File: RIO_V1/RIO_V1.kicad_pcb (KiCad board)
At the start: 2 copper layers, 34 x 34 mm, 9 parts, among them J1 POGO_Conn, SW1 TL1105SF160Q, SW2 TL1105SF160Q, U2 NanoS3

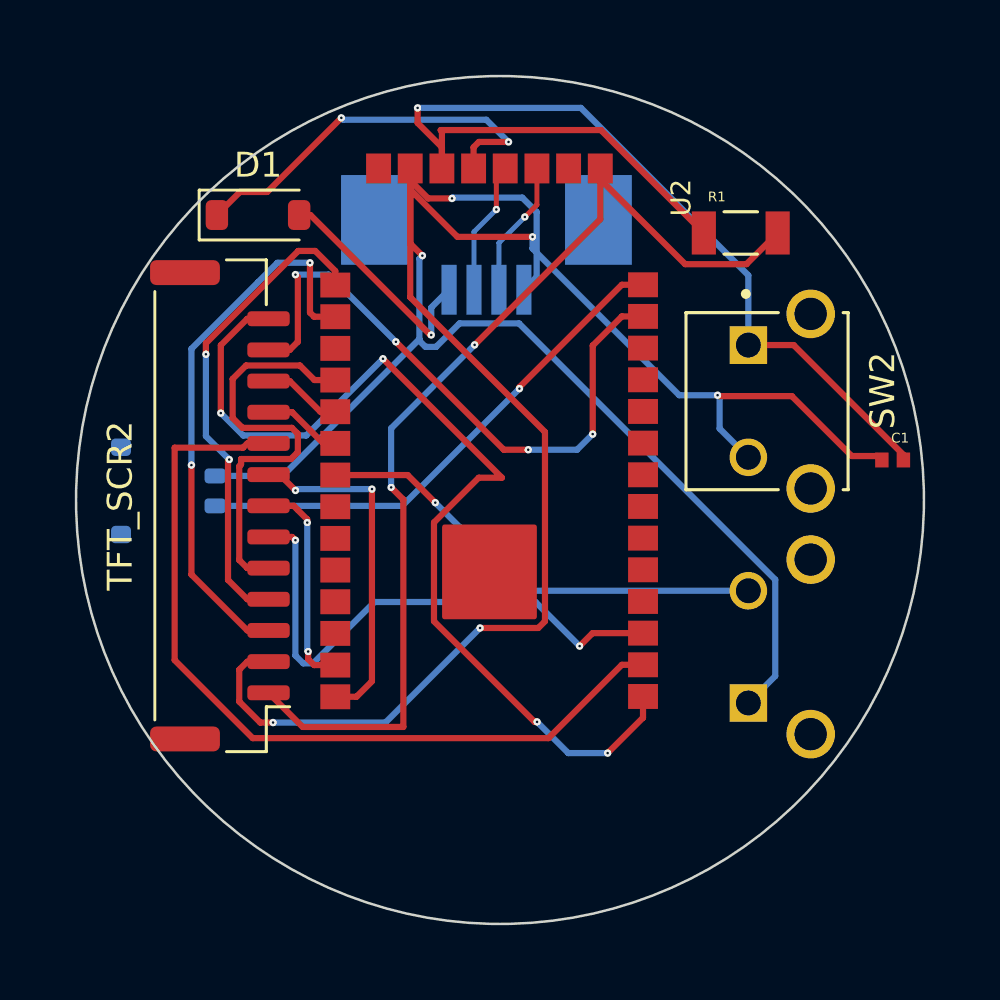
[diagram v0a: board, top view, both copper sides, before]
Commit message: Updated Symbols Footrprints and Routing
Updated the symbols, footprints and the PCB routing to work with the new resistors and ADC circuit
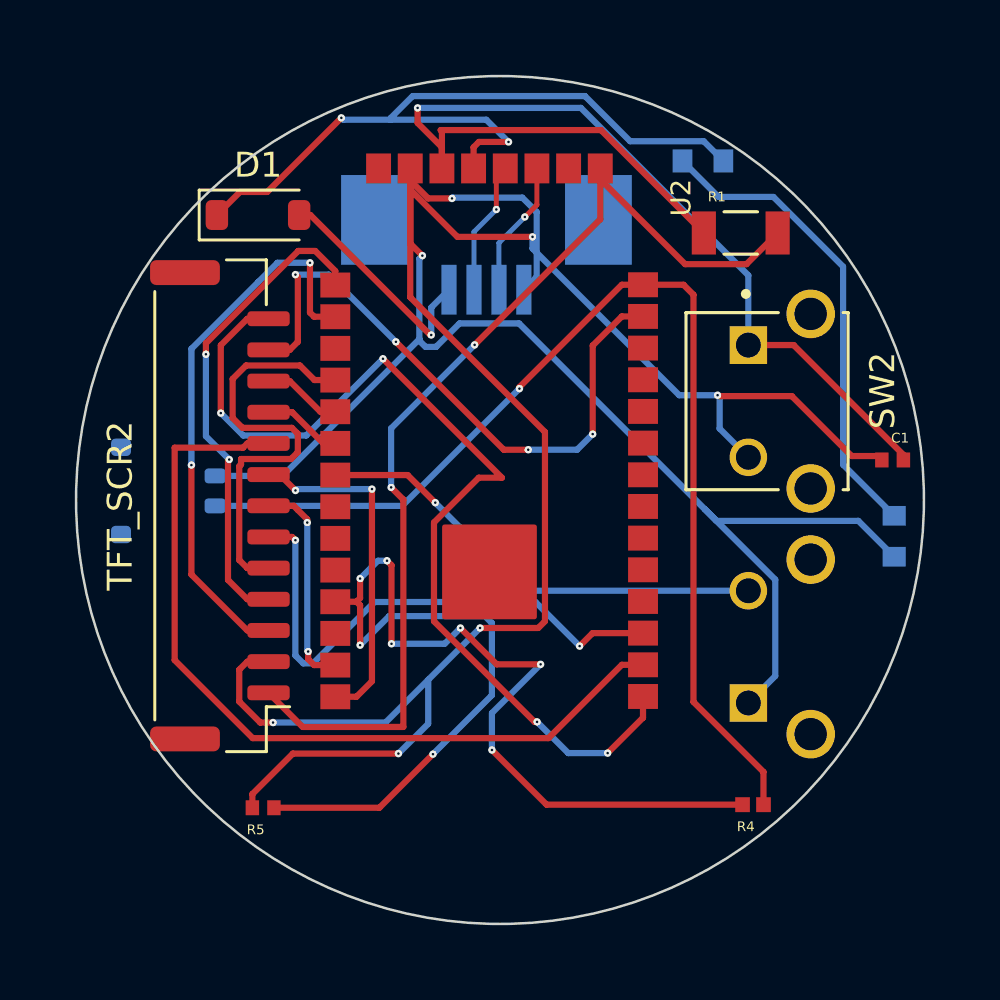
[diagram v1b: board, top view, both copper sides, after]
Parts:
- added R2: 50k, RT0603BRD0750KL:RESC1608X55N, B.Cu at (140.4, 80.4)
- added R3: 50k, RT0603BRD0750KL:RESC1608X55N, B.Cu at (148.1, 95.4)
- added R4: 442k, RMCF0402FT442K:RESC1005X35N, F.Cu at (142.4, 106.2)
- added R5: 160k, RC0402FR-07160KL:RESC1005X40N, F.Cu at (122.8, 106.3)
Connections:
- U2 pad 1: unconnected-(U2-STAT-Pad1) -> STAT
- U2 pad 33: unconnected-(U2-IO1-Pad33) -> IO1
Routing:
- net IO1: track 0.00 -> 49.8 mm, vias 0 -> 8
- net VBAT: track 20.9 -> 44.7 mm
- net IO17: track 0.00 -> 19.0 mm
- net GND: track 116.1 -> 135.0 mm, vias 6 -> 7
- net +5V: track 16.0 -> 30.9 mm

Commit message: Changed The FPC Connector To A Smaller Pitch
Changed the FPC connector on the PCB so that the pitch is reduced and overall footprint is minimized as much as possible
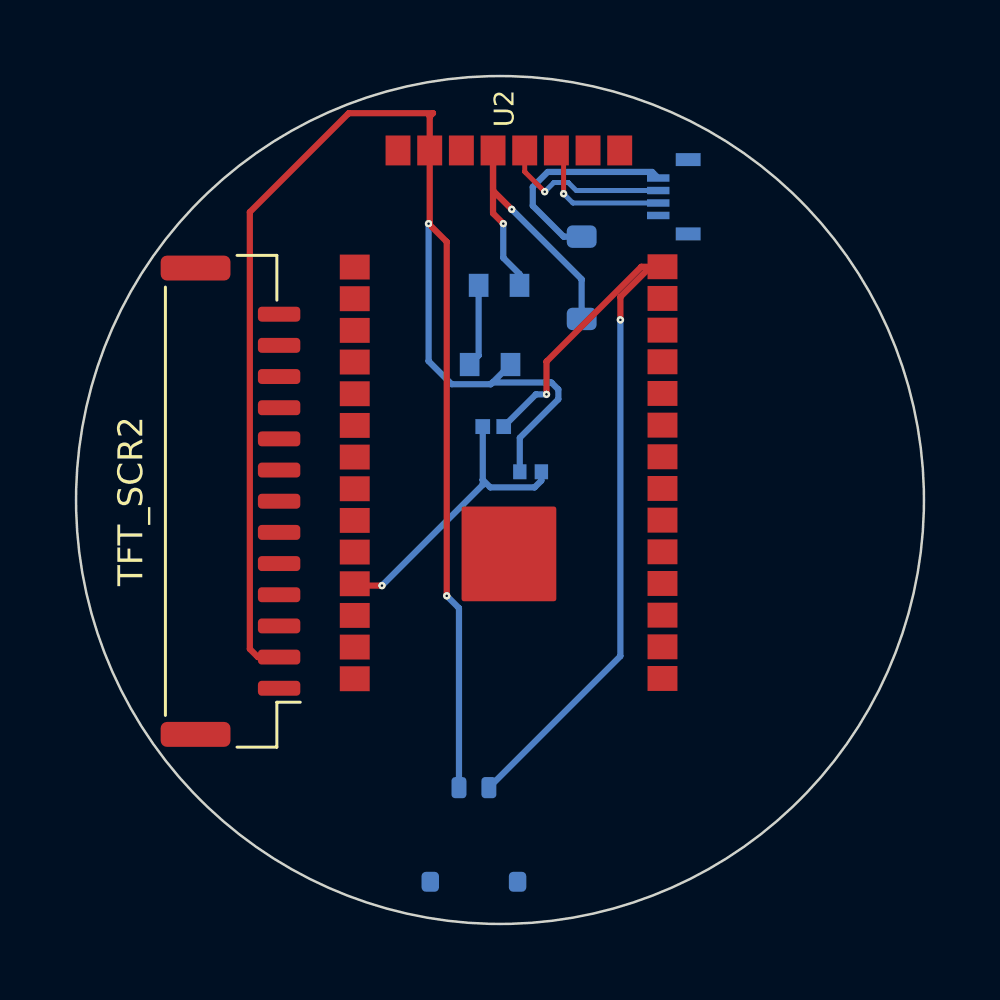
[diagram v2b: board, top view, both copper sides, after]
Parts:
- removed C1: JMK105BJ105KV-F, JMK105BJ105KV-F:CAPC1005X55N
- removed R1: RC1206FR-0710KL, RC1206FR-0710KL:RESC3116X65N
- removed SW1, SW2: TL1105SF160Q, TL1105SF160Q:SW_TL1105SF160Q
- D1, R4, R5: moved to B.Cu
- J1: footprint Connector_FFC-FPC:TE_84952-4_1x04-1MP_P1.0mm_Horizontal -> Connector:AMPHENOL_59453-042110ECHLF
- moved BT2 18.4 mm to (131.2, 107.4), turned to 180 degrees
- moved R4 18.4 mm to (132.0, 91.0)
- moved R3 17.6 mm to (131.9, 88.5), turned to 0 degrees
- moved R5 17.2 mm to (133.5, 92.8)
- moved D1 13.2 mm to (135.6, 85.1), turned to 90 degrees
- moved R2 9.58 mm to (132.2, 85.4)
- moved J1 8.32 mm to (139.8, 81.8), turned to -90 degrees
- moved U2 1.06 mm to (126.4, 79.9)
- moved TFT_SCR2 0.46 mm to (121.5, 94.0)
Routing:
- net GND: track 135.0 -> 71.7 mm, vias 7 -> 2
- net RESET: track 43.7 -> 0.00 mm, vias 1 -> 0
- net +3V3: track 41.5 -> 0.00 mm, vias 2 -> 0
- net IO5: track 39.4 -> 0.00 mm, vias 4 -> 0
- net IO1: track 49.8 -> 12.1 mm, vias 8 -> 1
- net IO6: track 33.7 -> 0.00 mm
- net IO21: track 25.2 -> 0.00 mm, vias 4 -> 0
- net IO37: track 22.3 -> 0.00 mm, vias 2 -> 0
- net IO7: track 21.8 -> 0.00 mm, vias 2 -> 0
- net IO35: track 19.5 -> 0.00 mm, vias 2 -> 0
- net IO0: track 18.5 -> 0.00 mm, vias 1 -> 0
- net IO34: track 17.5 -> 0.00 mm
- net +5V: track 30.9 -> 14.1 mm
- net IO17: track 19.0 -> 3.33 mm
- net IO4: track 13.9 -> 0.00 mm, vias 2 -> 0
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
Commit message: Added New PCB Conenctors, Routes, Components
Added new PCB components to reduce the height, changed the traces and adjusted for the battery in the PCB
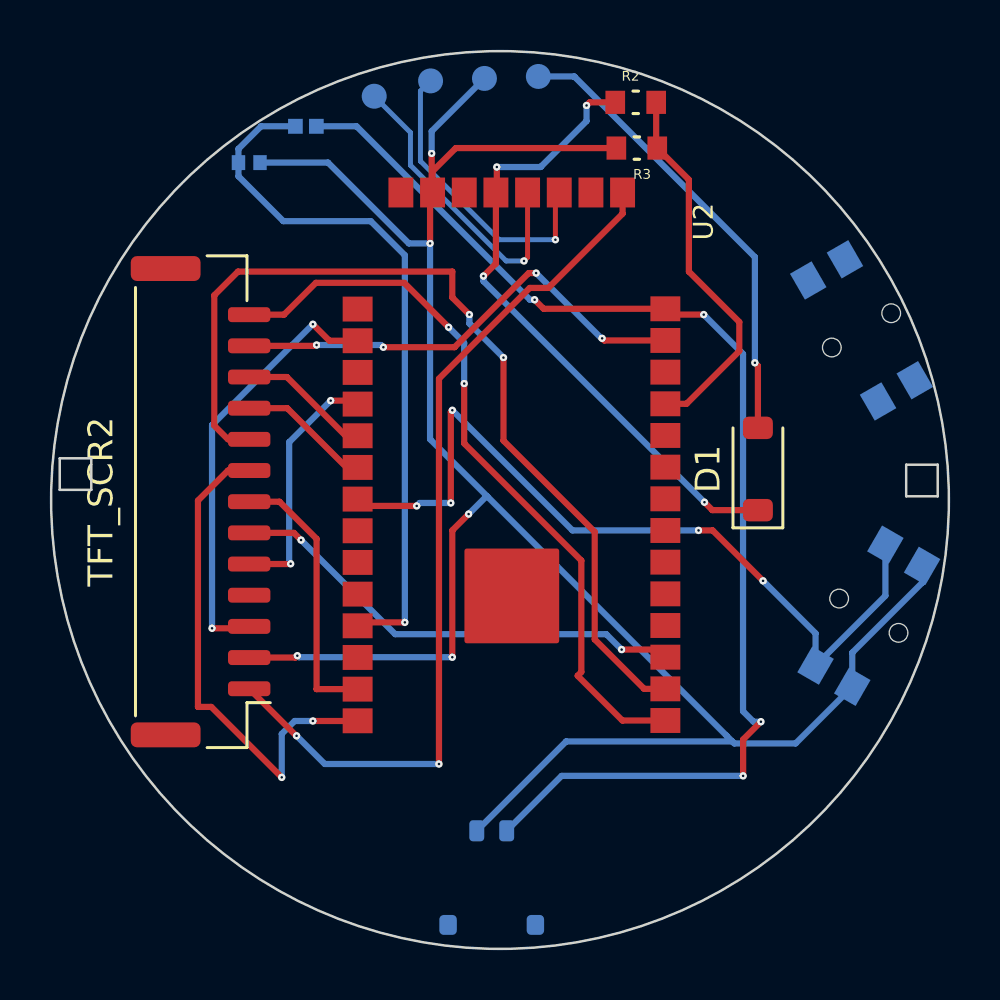
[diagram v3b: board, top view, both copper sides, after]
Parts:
- removed BT2: Battery, Connector_JST:JST_ACH_BM02B-ACHSS-GAN-ETF_1x02-1MP_P1.20mm_Vertical
- removed J1: POGO_Conn, Connector:AMPHENOL_59453-042110ECHLF
- added +: TestPoint, TestPoint:TestPoint_Pad_D1.0mm, B.Cu at (133.8, 77.0)
- added -: TestPoint, TestPoint:TestPoint_Pad_D1.0mm, B.Cu at (131.7, 77.1)
- added BT1: Battery, Connector_JST:JST_ACH_BM02B-ACHSS-GAN-ETF_1x02-1MP_P1.20mm_Vertical, B.Cu at (131.9, 109.1)
- added D+: TestPoint, TestPoint:TestPoint_Pad_D1.0mm, B.Cu at (129.5, 77.2)
- added D-: TestPoint, TestPoint:TestPoint_Pad_D1.0mm, B.Cu at (127.2, 77.8)
- added S1: TL1014BF160QG, TL1014BF160QG:TL1014BF160QG, B.Cu at (147.3, 87.0)
- added S2: TL1014BF160QG, TL1014BF160QG:TL1014BF160QG, B.Cu at (147.4, 99.0)
- D1, R2, R3: moved to F.Cu
- moved R5 16.8 mm to (122.2, 80.4), turned to 0 degrees
- moved R4 14.2 mm to (124.5, 79.0)
- moved R3 10.5 mm to (137.8, 79.9), turned to 180 degrees
- moved D1 10.4 mm to (142.6, 92.7)
- moved R2 9.16 mm to (137.7, 78.0), turned to 0 degrees
- moved U2 1.69 mm to (126.5, 81.5)
- moved TFT_SCR2 1.20 mm to (120.3, 94.0)
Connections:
- U2 pad 12: unconnected-(U2-IO17-Pad12) -> IO17
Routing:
- net IO6: track 0.00 -> 37.6 mm, vias 0 -> 2
- net +3V3: track 0.00 -> 35.3 mm, vias 0 -> 2
- net IO0: track 0.00 -> 33.2 mm, vias 0 -> 5
- net IO5: track 0.00 -> 29.8 mm, vias 0 -> 2
- net IO4: track 0.00 -> 20.4 mm, vias 0 -> 2
- net IO21: track 0.00 -> 19.1 mm, vias 0 -> 4
- net IO7: track 0.00 -> 18.8 mm, vias 0 -> 2
- net IO37: track 0.00 -> 17.5 mm, vias 0 -> 2
- net GND: track 71.7 -> 88.1 mm, vias 2 -> 5
- net IO1: track 12.1 -> 28.4 mm
- net VBAT: track 33.8 -> 49.0 mm, vias 2 -> 4
- net IO17: track 3.33 -> 15.2 mm
- net +5V: track 14.1 -> 25.8 mm, vias 2 -> 4
- net IO3: track 0.00 -> 11.0 mm
- net IO34: track 0.00 -> 10.1 mm, vias 0 -> 2
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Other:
- board size 34 x 34 mm -> 36 x 36 mm
